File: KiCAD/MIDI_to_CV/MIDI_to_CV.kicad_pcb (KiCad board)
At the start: 2 copper layers, 30 x 100 mm, 18 parts, among them J1 GATE, J2 DIN-5_180degree, J3 PITCH, J4 Conn_01x03_Socket, J5 Conn_01x03_Socket, U1 ATtiny45-20P, U2 6N138, U3 L7805

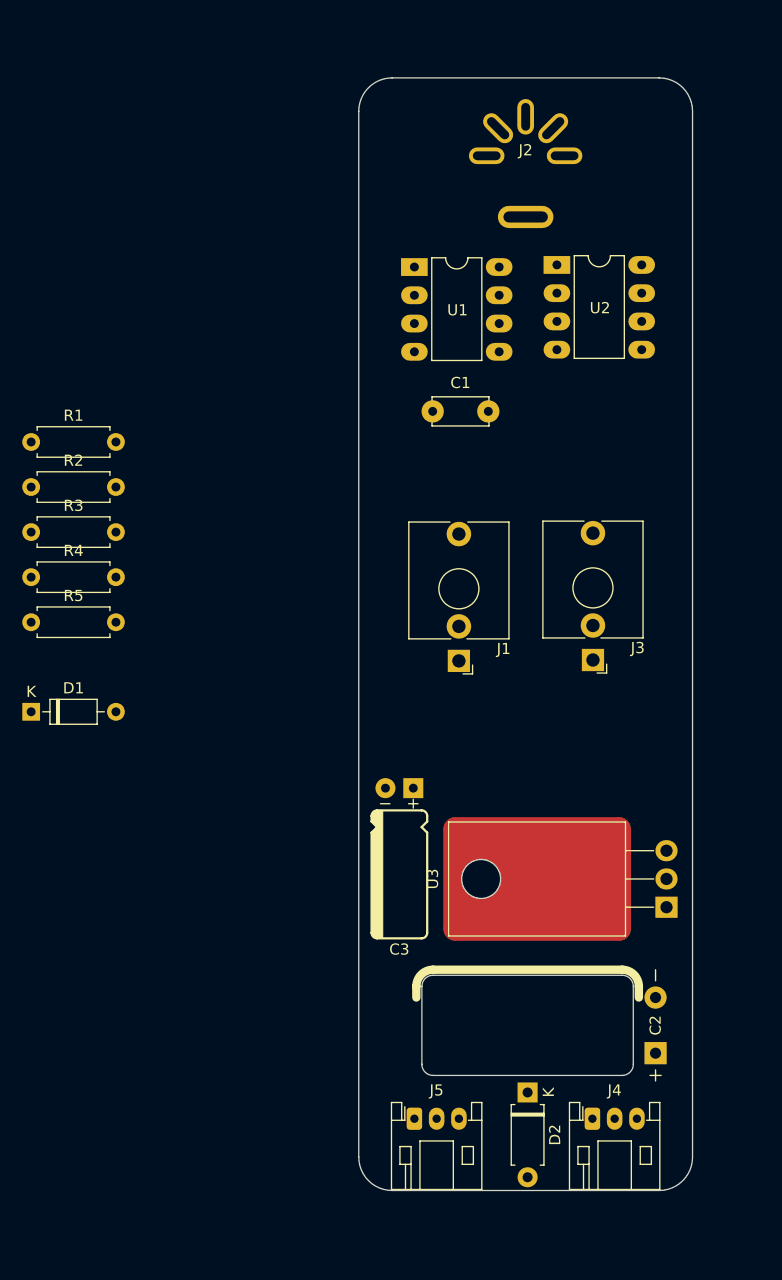
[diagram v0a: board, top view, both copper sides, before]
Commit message: MIDI to CV - PCB Placement
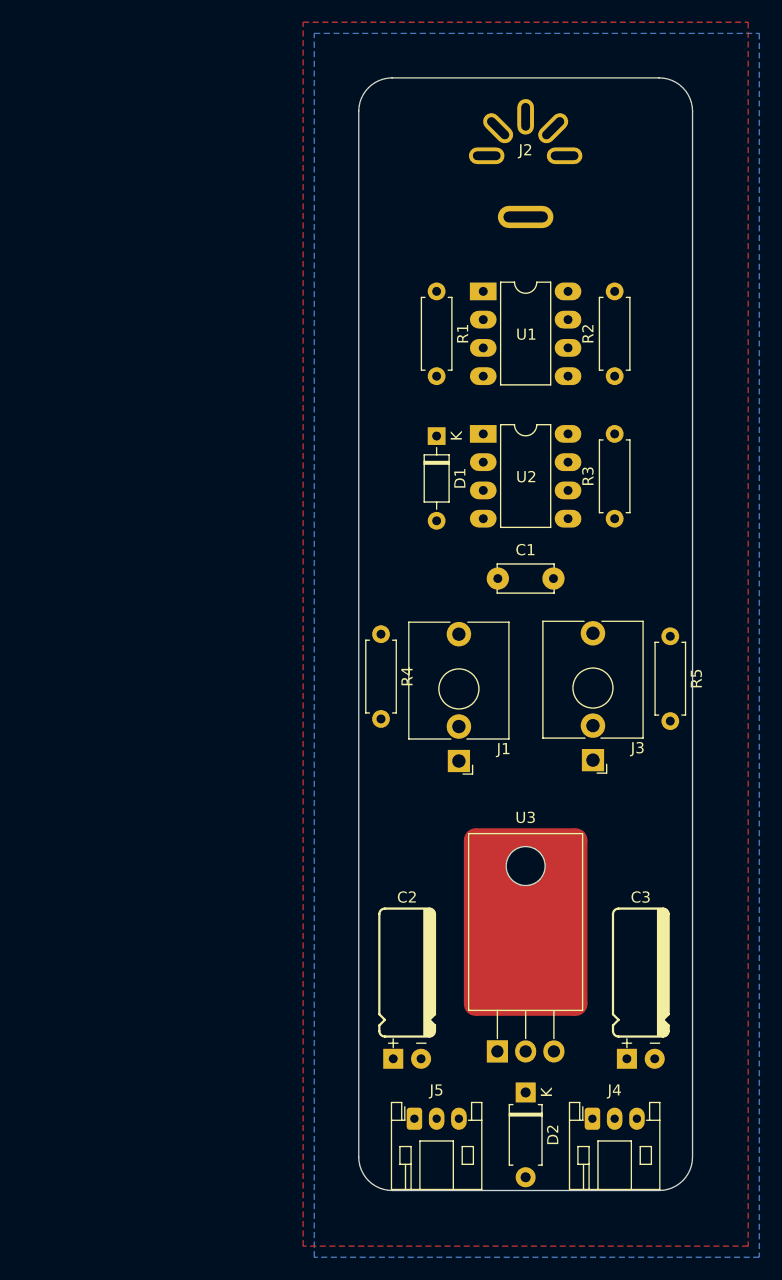
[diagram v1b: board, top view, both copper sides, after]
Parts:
- C2: value 470uF -> 10uF 10v; footprint HackSynth:CP_Radial_D10.0mm_P5.00mm_MidMount -> HackSynth:CP_Radial_D5.2mm_P2.50mm_LayDown
- C3: value 1uF -> 1uF 10v
- moved R5 57.5 mm to (178.0, 100.2), turned to -90 degrees
- moved R2 53.4 mm to (173.0, 76.8), turned to 90 degrees
- moved R3 52.5 mm to (173.0, 89.6), turned to 90 degrees
- moved D1 44.1 mm to (157.0, 82.2), turned to -90 degrees
- moved R1 38.9 mm to (157.0, 69.2), turned to -90 degrees
- moved C3 32.6 mm to (175.3, 138.2), turned to 0 degrees
- moved R4 31.9 mm to (152.0, 100.0), turned to -90 degrees
- moved C2 22.3 mm to (154.3, 138.2), turned to 0 degrees
- moved U3 20.0 mm to (165.0, 137.5), turned to 0 degrees
- moved U2 16.6 mm to (165.0, 85.8)
- moved C1 16.1 mm to (162.5, 95.0)
- moved J1 9.00 mm to (159.0, 104.9)
- moved J3 9.00 mm to (171.1, 104.8)
- moved U1 6.57 mm to (165.0, 73.0)
- moved D2 0.18 mm to (165.0, 141.2)
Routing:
- added copper zone on B.Cu, net +5V
- added copper zone on F.Cu, net GND

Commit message: MIDI to CV - PCB
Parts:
- added Ref**: Val**, HackSynth:CCHS Logo - 10mm, B.Cu at (158.5, 128.5)
- added Ref**: Val**, HackSynth:PancakeLegend Logo - 10mm, B.Cu at (171.5, 128.5)
- moved D2 0.44 mm to (165.0, 140.8)
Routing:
- net Net-(D1-A): track 0.00 -> 41.5 mm
- net Net-(U1-PB2): track 0.00 -> 35.0 mm
- net Net-(U1-PB1): track 0.00 -> 34.2 mm
- net VSS: track 0.00 -> 23.6 mm
- net VDD: track 0.00 -> 22.7 mm
- net Net-(C1-Pad1): track 0.00 -> 19.8 mm
- net Net-(J2-Pad4): track 0.00 -> 19.0 mm
- net Net-(D2-K): track 0.00 -> 16.9 mm
- net PB0: track 0.00 -> 16.3 mm
- net Net-(J3-PadT): track 0.00 -> 11.9 mm
- net Net-(D1-K): track 0.00 -> 10.5 mm
- net Net-(U2-VO1): track 0.00 -> 5.24 mm

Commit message: MIDI to CV - PCB
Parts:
- J1: value GATE -> DIN-5_180degree; footprint HackSynth:Jack_3.5mm -> HackSynth:DIN-5 - DS-5-07A - MIDI Jack
- J2: value DIN-5_180degree -> GATE; footprint HackSynth:DIN-5 MIDI Jack -> HackSynth:Jack_3.5mm
- moved J2 48.5 mm to (158.0, 105.0)
- moved J1 47.3 mm to (165.0, 58.0)
- moved R5 18.9 mm to (173.0, 82.0)
- moved R4 18.7 mm to (157.0, 82.0)
- moved J4 16.0 mm to (155.0, 143.5)
- moved J5 16.0 mm to (171.0, 143.6)
- moved R3 4.00 mm to (177.0, 89.5)
- moved D1 4.00 mm to (153.0, 82.2)
- moved J3 0.96 mm to (172.0, 105.0)
- moved Ref** 0.10 mm to (171.5, 128.4)
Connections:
- R1 pad 1: Net-(J2-Pad4) -> Net-(J1-Pad4)
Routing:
- net Net-(J2-Pad4): track 19.0 -> 0.00 mm
- net Net-(U1-PB2): track 35.0 -> 16.6 mm
- net Net-(U1-PB1): track 34.2 -> 15.7 mm
- net Net-(J1-Pad4): track 0.00 -> 18.0 mm
- net Net-(D1-K): track 10.5 -> 16.2 mm
- net Net-(U2-VO1): track 5.24 -> 9.29 mm
- net Net-(C1-Pad1): track 19.8 -> 16.5 mm
- net Net-(D1-A): track 41.5 -> 44.5 mm
- net Net-(J3-PadT): track 11.9 -> 10.9 mm
- net VDD: track 22.7 -> 22.0 mm
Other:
- board text added: "GATE"
- board text added: "MIDI to CV v1-0"
- board text added: "PITCH"
- board text added: "Pancake Legend 2025"

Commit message: MIDI Jack Footprint
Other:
- board text added: "PancakeLegend 2025"
- board text removed: "Pancake Legend 2025"
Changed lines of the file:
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@@
 			(layer "F.CrtYd")
+		)
+		(fp_circle
+			(center 0 0)
+			(end 0 -8)
+			(stroke
+				(width 0.1)
+				(type default)
+			)
+			(fill no)
+			(layer "F.Fab")
 		)
 		(fp_text user "${REFERENCE}"
@@
 		)
 	)
-	(gr_text "Pancake Legend 2025"
-		(at 152.5 116 270)
+	(gr_text "PancakeLegend 2025"
+		(at 152.5 115 270)
 		(layer "B.SilkS")
 		(effects
@@
 	)
 	(gr_text "MIDI to CV v1-0"
-		(at 176.25 114 270)
+		(at 176.25 113 270)
 		(layer "B.SilkS")
 		(effects

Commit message: MIDI to CV - Gerbers
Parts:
- C2: value 10uF 10v -> 10uF 25v
- C3: value 1uF 10v -> 1uF 50v
- J2: value GATE -> PITCH
- J3: value PITCH -> GATE
- moved R4 23.2 mm to (177.0, 70.2)
- moved C1 21.3 mm to (173.0, 76.5), turned to 90 degrees
- moved R2 21.1 mm to (157.0, 90.6)
- moved J2 14.2 mm to (172.0, 102.9)
- moved J3 14.2 mm to (158.0, 102.9)
- moved R1 1.00 mm to (157.0, 70.2)
- moved R3 1.00 mm to (177.0, 90.5)
- moved R5 1.00 mm to (173.0, 83.0)
- moved U1 1.00 mm to (165.0, 74.0)
- moved U2 1.00 mm to (165.0, 86.8)
- moved D1 0.71 mm to (153.0, 82.9)
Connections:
- J1 pad 2: unconnected-(J1-Pad2) -> GND
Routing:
- net Net-(C1-Pad1): track 16.5 -> 34.7 mm
- net PB0: track 16.3 -> 27.5 mm
- net Net-(J3-PadT): track 10.9 -> 18.1 mm
- net Net-(U1-PB1): track 15.7 -> 11.6 mm
- net Net-(J1-Pad4): track 18.0 -> 19.0 mm
- net Net-(D1-A): track 44.5 -> 45.4 mm
- net Net-(U1-PB2): track 16.6 -> 16.0 mm

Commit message: Mixer PCB - Gerbers
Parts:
- added REF**: Untitled, HackSynth:Module 30x100mm, F.Cu at (165.0, 100.0)
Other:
- board text added: "MIDI to CV v1-1"
- board text removed: "MIDI to CV v1-0"
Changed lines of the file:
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@@
 	)
 	(paper "A4")
+	(title_block
+		(title "MIDI to CV")
+		(date "2025-06-14")
+		(rev "1-1")
+	)
 	(layers
 		(0 "F.Cu" signal)
@@
 		)
 	)
+	(footprint "HackSynth:Module 30x100mm"
+		(layer "F.Cu")
+		(at 165 100)
+		(property "Reference" "REF**"
+			(at 0 -0.5 0)
+			(unlocked yes)
+			(layer "F.SilkS")
+			(hide yes)
+			(effects
+				(font
+					(size 1 1)
+					(thickness 0.1)
+				)
+			)
+		)
+		(property "Value" "Untitled"
+			(at 0 1 0)
+			(unlocked yes)
+			(layer "F.Fab")
+			(hide yes)
+			(effects
+				(font
+					(size 1 1)
+					(thickness 0.15)
+				)
+			)
+		)
+		(property "Datasheet" ""
+			(at 0 0 0)
+			(unlocked yes)
+			(layer "F.Fab")
+			(hide yes)
+			(effects
+				(font
+					(size 1 1)
+					(thickness 0.15)
+				)
+			)
+		)
+		(property "Description" ""
+			(at 0 0 0)
+			(unlocked yes)
+			(layer "F.Fab")
+			(hide yes)
+			(effects
+				(font
+					(size 1 1)
+					(thickness 0.15)
+				)
+			)
+		)
+		(attr smd)
+		(fp_line
+			(start -9 46)
+			(end -7 46)
+			(stroke
+				(width 0.1)
+				(type default)
+			)
+			(layer "Dwgs.User")
+		)
+		(fp_line
+			(start -8 45)
+			(end -8 47)
+			(stroke
+				(width 0.1)
+				(type default)
+			)
+			(layer "Dwgs.User")
+		)
+		(fp_line
+			(start 7 46)
+			(end 9 46)
+			(stroke
+				(width 0.1)
+				(type default)
+			)
+			(layer "Dwgs.User")
+		)
+		(fp_line
+			(start 8 45)
+			(end 8 47)
+			(stroke
+				(width 0.1)
+				(type default)
+			)
+			(layer "Dwgs.User")
+		)
+		(fp_line
+			(start -14.999999 -47)
+			(end -15 47)
+			(stroke
+				(width 0.05)
+				(type default)
+			)
+			(layer "Edge.Cuts")
+		)
+		(fp_line
+			(start -12 49.999999)
+			(end 12 50)
+			(stroke
+				(width 0.05)
+				(type default)
+			)
+			(layer "Edge.Cuts")
+		)
+		(fp_line
+			(start 12 -50)
+			(end -12 -50)
+			(stroke
+				(width 0.05)
+				(type default)
+			)
+			(layer "Edge.Cuts")
+		)
+		(fp_line
+			(start 15 47)
+			(end 15 -47)
+			(stroke
+				(width 0.05)
+				(type default)
+			)
+			(layer "Edge.Cuts")
+		)
+		(fp_arc
+			(start -15 -47)
+			(mid -14.12132 -49.12132)
+			(end -12 -50)
+			(stroke
+				(width 0.05)
+				(type default)
+			)
+			(layer "Edge.Cuts")
+		)
+		(fp_arc
+			(start -12 50)
+			(mid -14.12132 49.12132)
+			(end -15 47)
+			(stroke
+				(width 0.05)
+				(type default)
+			)
+			(layer "Edge.Cuts")
+		)
+		(fp_arc
+			(start 12 -50)
+			(mid 14.12132 -49.12132)
+			(end 15 -47)
+			(stroke
+				(width 0.05)
+				(type default)
+			)
+			(layer "Edge.Cuts")
+		)
+		(fp_arc
+			(start 15 47)
+			(mid 14.12132 49.12132)
+			(end 12 50)
+			(stroke
+				(width 0.05)
+				(type default)
+			)
+			(layer "Edge.Cuts")
+		)
+		(embedded_fonts no)
+	)
 	(footprint "Diode_THT:D_DO-35_SOD27_P7.62mm_Horizontal"
 		(layer "F.Cu")
@@
 		(embedded_fonts no)
 	)
-	(gr_arc
-		(start 180 147)
-		(mid 179.12132 149.12132)
-		(end 177 150)
-		(stroke
-			(width 0.05)
-			(type default)
-		)
-		(layer "Edge.Cuts")
-	)
-	(gr_line
-		(start 153 150)
-		(end 177 150)
-		(stroke
-			(width 0.05)
-			(type default)
-		)
-		(layer "Edge.Cuts")
-	)
-	(gr_arc
-		(start 150 53)
-		(mid 150.87868 50.87868)
-		(end 153 50)
-		(stroke
-			(width 0.05)
-			(type default)
-		)
-		(layer "Edge.Cuts")
-	)
-	(gr_line
-		(start 150 147)
-		(end 150 53)
-		(stroke
-			(width 0.05)
-			(type default)
-		)
-		(layer "Edge.Cuts")
-	)
-	(gr_line
-		(start 180 147)
-		(end 180 53)
-		(stroke
-			(width 0.05)
-			(type default)
-		)
-		(layer "Edge.Cuts")
-	)
-	(gr_line
-		(start 177 50)
-		(end 153 50)
-		(stroke
-			(width 0.05)
-			(type default)
-		)
-		(layer "Edge.Cuts")
-	)
-	(gr_arc
-		(start 177 50)
-		(mid 179.12132 50.87868)
-		(end 180 53)
-		(stroke
-			(width 0.05)
-			(type default)
-		)
-		(layer "Edge.Cuts")
-	)
-	(gr_arc
-		(start 153 150)
-		(mid 150.87868 149.12132)
-		(end 150 147)
-		(stroke
-			(width 0.05)
-			(type default)
-		)
-		(layer "Edge.Cuts")
-	)
 	(gr_text "GATE"
 		(at 158 113 0)
@@
 		)
 	)
-	(gr_text "MIDI to CV v1-0"
+	(gr_text "MIDI to CV v1-1"
 		(at 176.25 113 270)
 		(layer "B.SilkS")

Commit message: Review
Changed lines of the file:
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@@
 		)
 		(embedded_fonts no)
-		(model "C:/Program Files/KiCad/share/kicad/modules/packages3d/Package_DIP.3dshapes/DIP-8_W7.62mm.step"
+		(model "C:/Users/ocd/OneDrive/Drafting/CCHS/HackSynth/KiCAD/HackSynth.pretty/DIP-8_W7.62mm.step"
 			(offset
 				(xyz -3.81 3.81 0)
@@
 		(layer "F.Cu")
 		(at 153 82.94 -90)
-		(descr "Diode, DO-35_SOD27 series, Axial, Horizontal, pin pitch=7.62mm, , length*diameter=4*2mm^2, , http://www.diodes.com/_files/packages/DO-35.pdf")
+		(descr "Diode, DO-35_SOD27 series, Axial, Horizontal, pin pitch=7.62mm, length*diameter=4*2mm^2, http://www.diodes.com/_files/packages/DO-35.pdf")
 		(tags "Diode DO-35_SOD27 series Axial Horizontal pin pitch 7.62mm  length 4mm diameter 2mm")
 		(property "Reference" "D1"
@@
 		(attr through_hole)
 		(fp_line
-			(start 1.69 1.12)
-			(end 5.93 1.12)
-			(stroke
-				(width 0.12)
-				(type solid)
-			)
-			(layer "F.SilkS")
-		)
-		(fp_line
-			(start 5.93 1.12)
-			(end 5.93 -1.12)
-			(stroke
-				(width 0.12)
-				(type solid)
-			)
-			(layer "F.SilkS")
-		)
-		(fp_line
 			(start 1.04 0)
 			(end 1.69 0)
@@
 		)
 		(fp_line
-			(start 1.69 -1.12)
-			(end 1.69 1.12)
-			(stroke
-				(width 0.12)
-				(type solid)
-			)
-			(layer "F.SilkS")
-		)
-		(fp_line
 			(start 2.29 -1.12)
 			(end 2.29 1.12)
@@
 			(layer "F.SilkS")
 		)
-		(fp_line
-			(start 5.93 -1.12)
-			(end 1.69 -1.12)
-			(stroke
-				(width 0.12)
-				(type solid)
-			)
-			(layer "F.SilkS")
-		)
-		(fp_line
-			(start -1.05 1.25)
+		(fp_rect
+			(start 1.69 -1.12)
+			(end 5.93 1.12)
+			(stroke
+				(width 0.12)
+				(type solid)
+			)
+			(fill no)
+			(layer "F.SilkS")
+		)
+		(fp_rect
+			(start -1.05 -1.25)
 			(end 8.67 1.25)
 			(stroke
@@
 				(type solid)
 			)
+			(fill no)
 			(layer "F.CrtYd")
-		)
-		(fp_line
-			(start 8.67 1.25)
-			(end 8.67 -1.25)
-			(stroke
-				(width 0.05)
-				(type solid)
-			)
-			(layer "F.CrtYd")
-		)
-		(fp_line
-			(start -1.05 -1.25)
-			(end -1.05 1.25)
-			(stroke
-				(width 0.05)
-				(type solid)
-			)
-			(layer "F.CrtYd")
-		)
-		(fp_line
-			(start 8.67 -1.25)
-			(end -1.05 -1.25)
-			(stroke
-				(width 0.05)
-				(type solid)
-			)
-			(layer "F.CrtYd")
-		)
-		(fp_line
-			(start 1.81 1)
-			(end 5.81 1)
-			(stroke
-				(width 0.1)
-				(type solid)
-			)
-			(layer "F.Fab")
-		)
-		(fp_line
-			(start 5.81 1)
-			(end 5.81 -1)
-			(stroke
-				(width 0.1)
-				(type solid)
-			)
-			(layer "F.Fab")
 		)
 		(fp_line
@@
 		)
 		(fp_line
-			(start 1.81 -1)
-			(end 1.81 1)
-			(stroke
-				(width 0.1)
-				(type solid)
-			)
-			(layer "F.Fab")
-		)
-		(fp_line
 			(start 2.31 -1)
 			(end 2.31 1)
@@
 			(layer "F.Fab")
 		)
-		(fp_line
-			(start 5.81 -1)
-			(end 1.81 -1)
-			(stroke
-				(width 0.1)
-				(type solid)
-			)
+		(fp_rect
+			(start 1.81 -1)
+			(end 5.81 1)
+			(stroke
+				(width 0.1)
+				(type solid)
+			)
+			(fill no)
 			(layer "F.Fab")
 		)
@@
 			)
 		)
-		(pad "1" thru_hole rect
+		(pad "1" thru_hole roundrect
 			(at 0 0 270)
 			(size 1.6 1.6)
@@
 			(layers "*.Cu" "*.Mask")
 			(remove_unused_layers no)
+			(roundrect_rratio 0.15625)
 			(net 6 "Net-(D1-K)")
 			(pinfunction "K")
 			(pintype "passive")
 		)
-		(pad "2" thru_hole oval
+		(pad "2" thru_hole circle
 			(at 7.62 0 270)
 			(size 1.6 1.6)
@@
 		)
 		(embedded_fonts no)
-		(model "${KICAD9_3DMODEL_DIR}/Diode_THT.3dshapes/D_DO-35_SOD27_P7.62mm_Horizontal.wrl"
+		(model "${KICAD9_3DMODEL_DIR}/Diode_THT.3dshapes/D_DO-35_SOD27_P7.62mm_Horizontal.step"
 			(offset
 				(xyz 0 0 0)
@@
 		)
 		(embedded_fonts no)
-		(model "C:/Program Files/KiCad/share/kicad/modules/packages3d/Package_DIP.3dshapes/DIP-8_W7.62mm.step"
+		(model "C:/Users/ocd/OneDrive/Drafting/CCHS/HackSynth/KiCAD/HackSynth.pretty/DIP-8_W7.62mm.step"
 			(offset
 				(xyz -3.81 3.81 0)

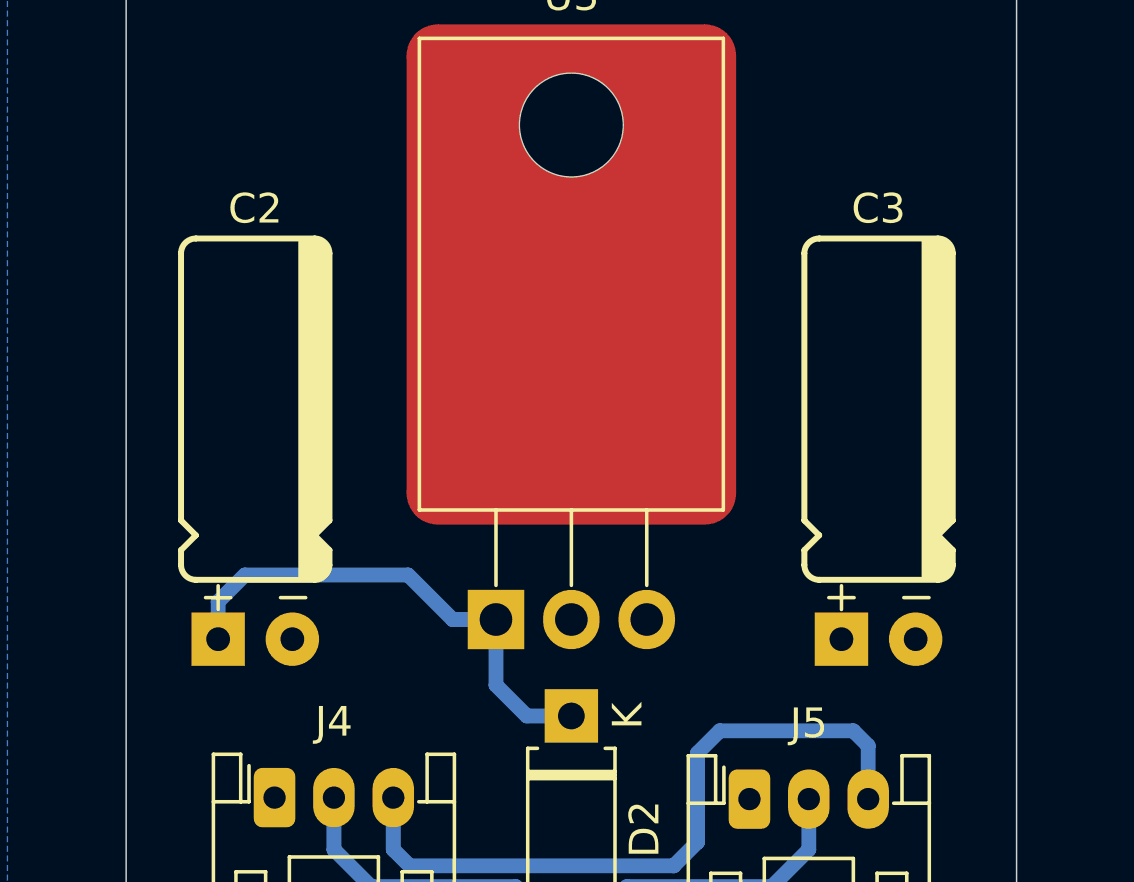
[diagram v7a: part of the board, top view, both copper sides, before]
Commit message: MIDI to CV Cap Footprint Change
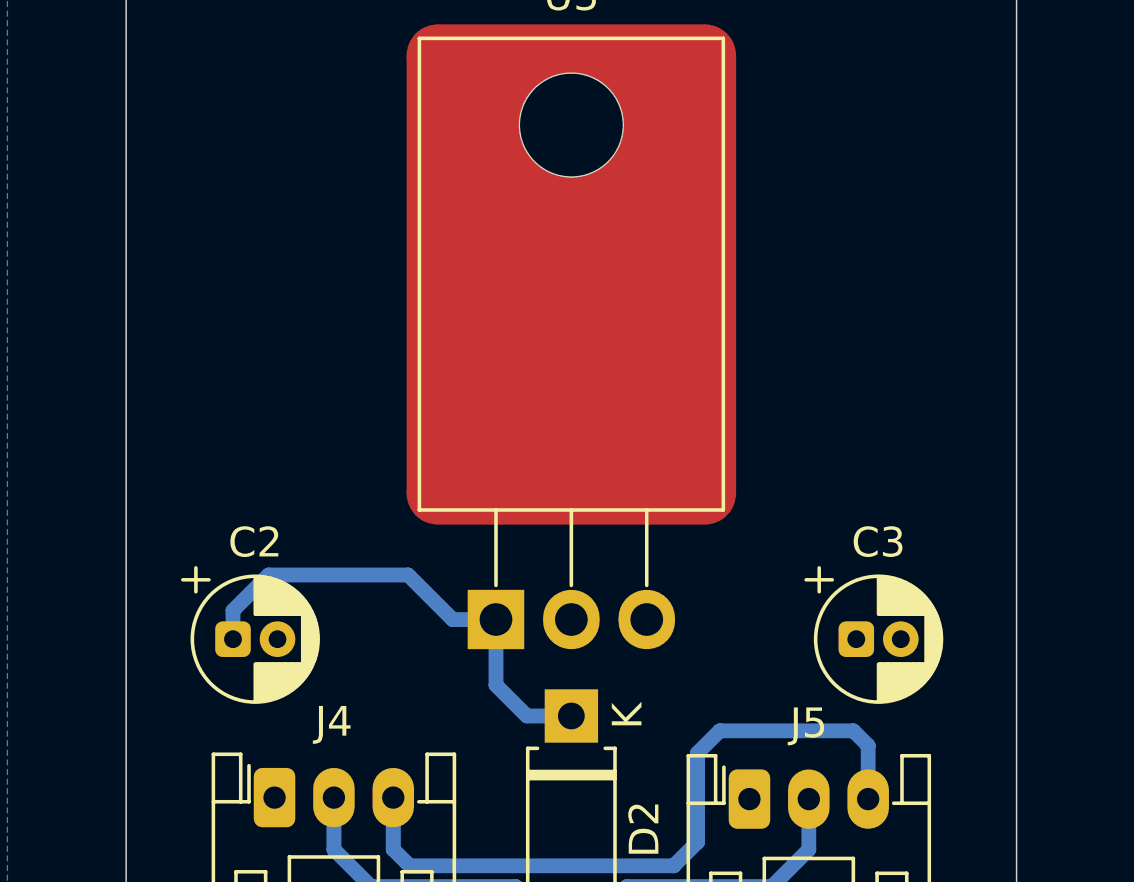
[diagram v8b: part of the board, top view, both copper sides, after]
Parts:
- C2, C3: footprint HackSynth:CP_Radial_D5.2mm_P2.50mm_LayDown -> HackSynth:CP_Radial_D4.0mm_P1.50mm
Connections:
- J1 pad G: GND -> (no net)
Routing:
- net Net-(D2-K): track 16.8 -> 16.1 mm
